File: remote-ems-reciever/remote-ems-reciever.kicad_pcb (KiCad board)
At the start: 2 copper layers, 50 x 50 mm, 43 parts, among them IC1 Wio-E5, IC2 MCP2562, J1 Conn_Coaxial, J2 Conn_01x04, J3 Conn_01x04, J4 Conn_01x04_Pin, J5 Conn_01x04, Q1 BSS138, SW1 SW_Push, SW2 SW_Push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

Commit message: remote-ems-reciever　ビア、シルク、LED以外完成
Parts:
- moved SW3 90.9 mm to (17.2, 39.4)
- moved SW2 71.4 mm to (32.5, 42.0), turned to 90 degrees
- moved C6 66.7 mm to (19.6, 35.6), turned to -90 degrees
- moved C10 62.8 mm to (32.2, 62.2), turned to 90 degrees
- moved C9 58.1 mm to (38.6, 62.2), turned to 90 degrees
- moved C8 57.5 mm to (34.4, 47.1), turned to -90 degrees
- moved R6 57.4 mm to (42.4, 59.5), turned to -90 degrees
- moved R4 55.1 mm to (35.2, 42.0)
- moved Q1 54.5 mm to (46.2, 30.0), turned to 90 degrees
- moved R3 51.3 mm to (40.8, 59.5), turned to -90 degrees
- moved D1 51.2 mm to (40.8, 62.9), turned to 90 degrees
- moved D2 49.0 mm to (42.4, 62.9), turned to 90 degrees
- moved R5 48.2 mm to (46.1, 32.8)
- moved C1 47.3 mm to (38.4, 34.9), turned to 90 degrees
- moved C5 45.3 mm to (40.4, 40.8), turned to 90 degrees
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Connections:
- U1 pad 10: DIP2 -> unconnected-(U1-PA5-Pad10)
- U1 pad 25: unconnected-(U1-PA15-Pad25) -> LED2
- U1 pad 26: unconnected-(U1-PB3-Pad26) -> LED1
- U1 pad 27: LED1 -> DIP1
- U1 pad 28: LED2 -> DIP2
- U1 pad 9: DIP1 -> unconnected-(U1-PA4-Pad9)
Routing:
- net +3.3V: track 6.05 -> 128.9 mm, vias 0 -> 5
- net +5V: track 0.00 -> 52.7 mm, vias 0 -> 3
- net CANL: track 0.00 -> 35.6 mm
- net Net-(IC1-RST): track 0.00 -> 34.1 mm, vias 0 -> 2
- net UART_TX: track 0.00 -> 30.9 mm, vias 0 -> 1
- net CANH: track 0.00 -> 30.7 mm
- net UART_RX: track 0.00 -> 29.1 mm, vias 0 -> 1
- net Wio_RX: track 0.00 -> 21.0 mm, vias 0 -> 2
- net Wio_TX: track 0.00 -> 20.2 mm, vias 0 -> 2
- net DIP1: track 2.46 -> 22.1 mm, vias 0 -> 1
- net SWDIO: track 0.00 -> 17.9 mm
- net DIP2: track 2.44 -> 17.1 mm, vias 0 -> 1
- net SWCLK: track 0.00 -> 14.2 mm
- net NRST: track 0.00 -> 14.0 mm
- net CAN_TX: track 0.00 -> 10.6 mm
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
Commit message: ビア打ち、シルク修正中　残りは別日に対応します
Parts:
- moved D2 12.3 mm to (30.2, 61.0)
- moved R6 12.3 mm to (30.2, 57.6)
- moved D1 12.3 mm to (28.6, 61.0)
- moved R3 12.3 mm to (28.6, 57.6)
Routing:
- net +3.3V: track 128.9 -> 117.3 mm
- net +5V: track 52.7 -> 55.1 mm
- net GNDD: vias 2 -> 28
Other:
- board text added: "3.3 5"

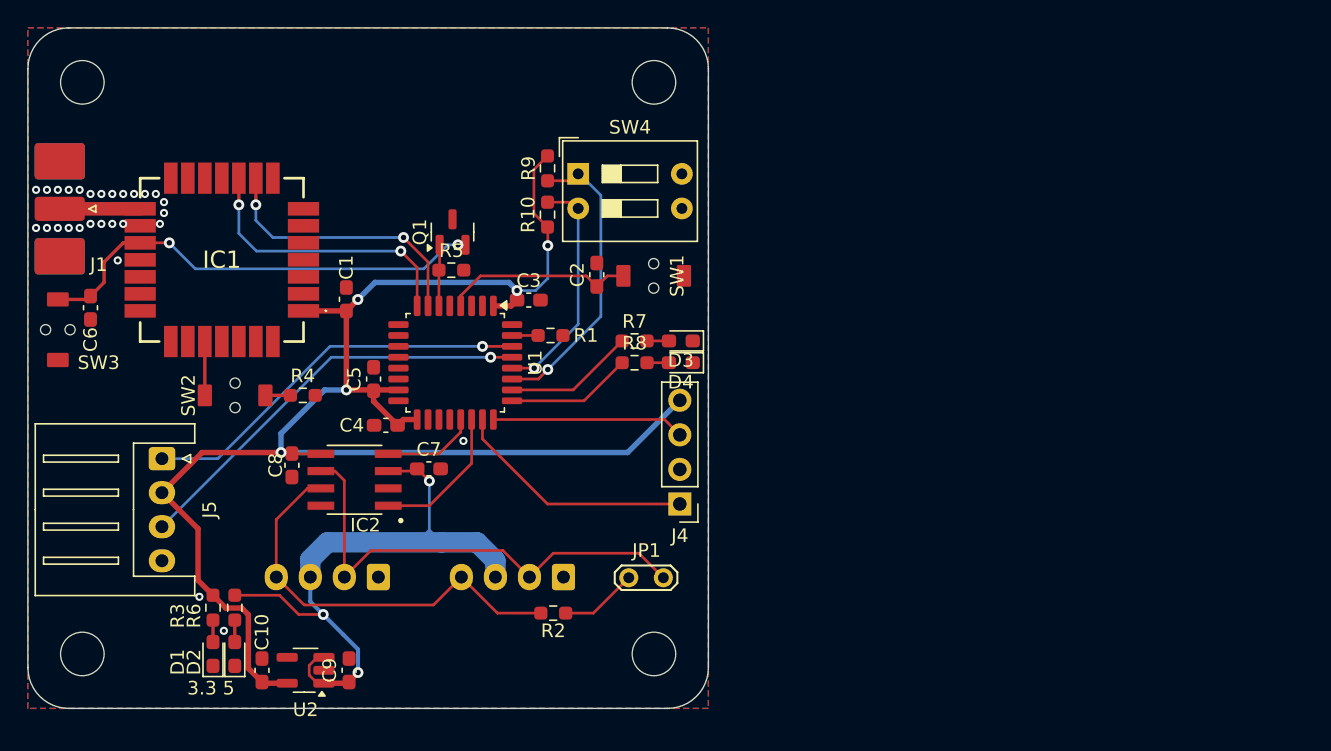
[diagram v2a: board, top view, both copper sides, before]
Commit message: FETの向きを修正 ガーバー出力
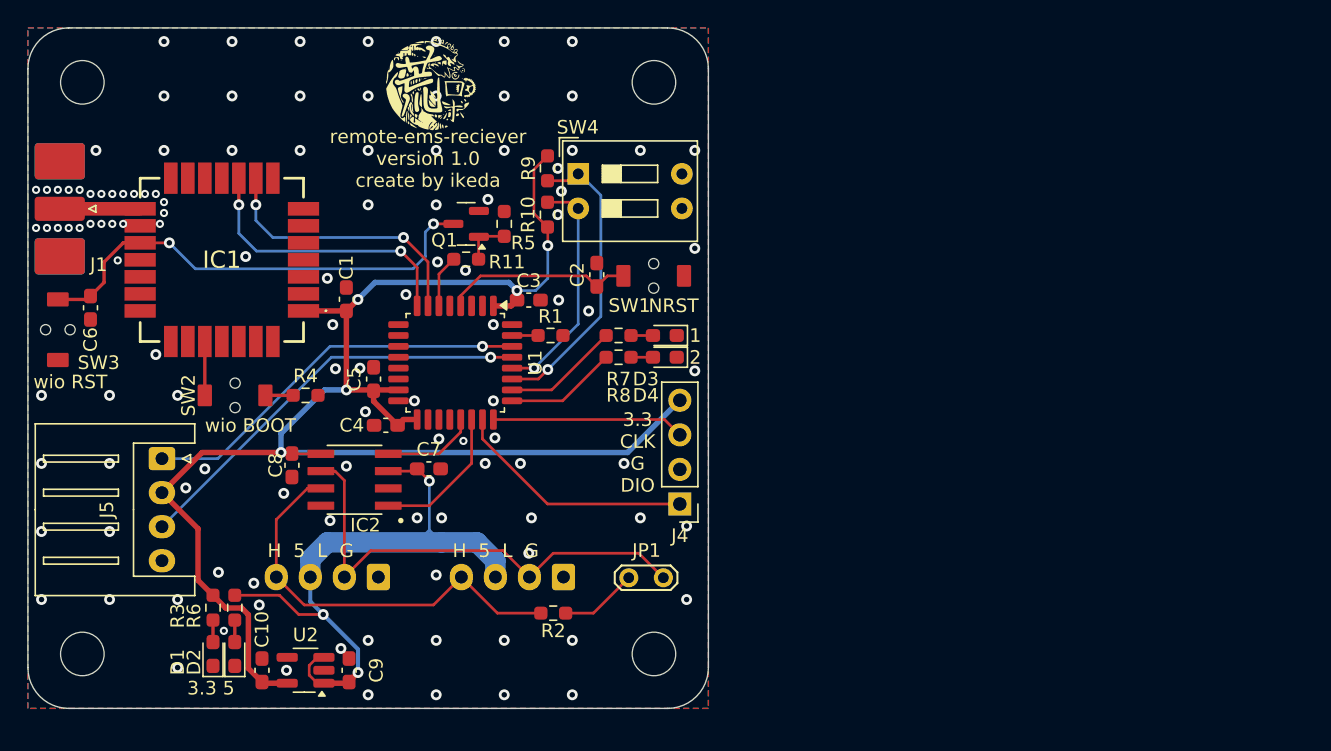
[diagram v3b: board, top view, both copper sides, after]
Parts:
- added G***: LOGO, LOGO, F.Cu at (44.4, 19.4)
- added R11: 100, Resistor_SMD:R_0603_1608Metric_Pad0.98x0.95mm_HandSolder, F.Cu at (47.2, 32.0)
- moved R5 5.16 mm to (50.0, 29.4), turned to 90 degrees
- moved D3 1.24 mm to (61.8, 37.6)
- moved D4 1.24 mm to (61.8, 39.2)
- moved R7 1.24 mm to (58.4, 37.6)
- moved R8 1.24 mm to (58.4, 39.2)
- moved Q1 1.17 mm to (47.2, 29.4), turned to 180 degrees
- moved R4 0.20 mm to (35.4, 42.0)
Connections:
- Q1 pad 1: Wio-RST -> Net-(Q1-G)
- Q1 pad 2: Net-(IC1-RST) -> GNDD
- Q1 pad 3: GNDD -> Net-(IC1-RST)
- R5 pad 1: Wio-RST -> Net-(Q1-G)
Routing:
- net Net-(Q1-G): track 0.00 -> 3.54 mm
- net LED1: track 9.58 -> 8.57 mm
- net LED2: track 9.25 -> 8.24 mm
- net Net-(IC1-RST): track 34.1 -> 34.9 mm
- net Wio-RST: track 4.51 -> 3.88 mm
- net GNDD: vias 28 -> 116
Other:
- board text added: "1 2"
- board text added: "3.3 CLK G DIO"
- board text added: "H 5 L G"
- board text added: "NRST"
- board text added: "remote-ems-reciever version 1.0 create by ikeda"
- board text added: "wio BOOT"
- board text added: "wio RST"
